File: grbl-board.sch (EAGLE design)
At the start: 29 parts, among them IC2 FT232RL, IC3 ADUM1250, IC4 LM2596S, X1 PN61729-S, X5 22-23-2021

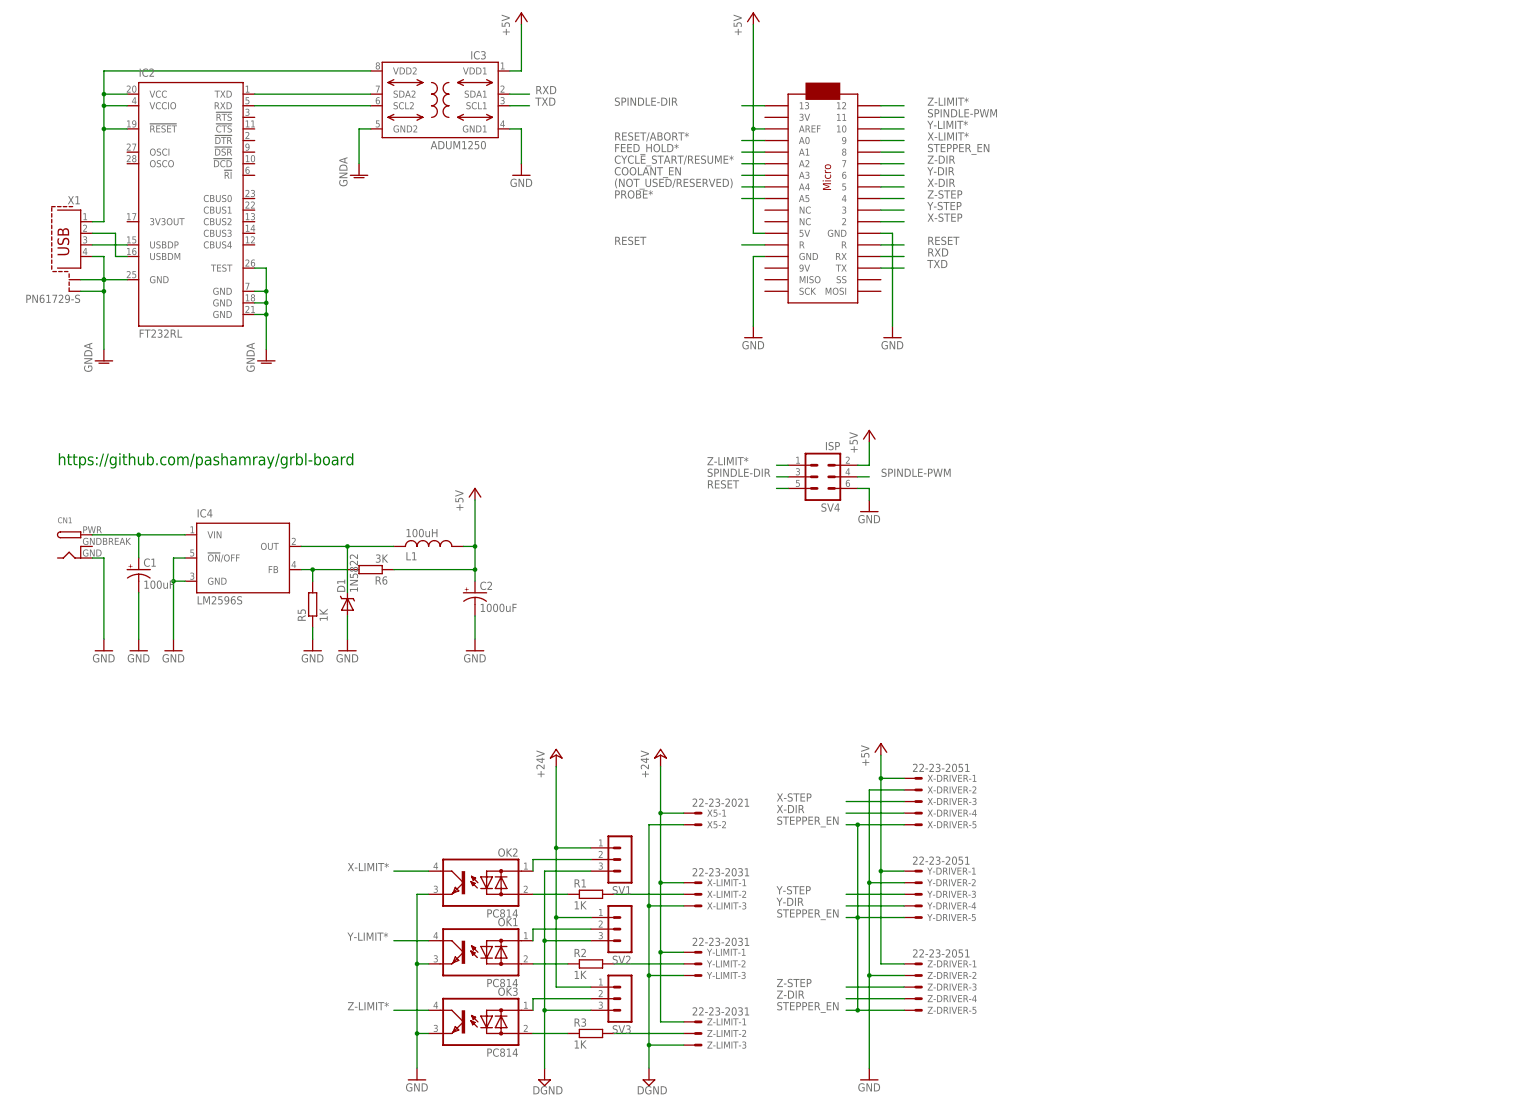
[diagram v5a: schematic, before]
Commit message: del arduino
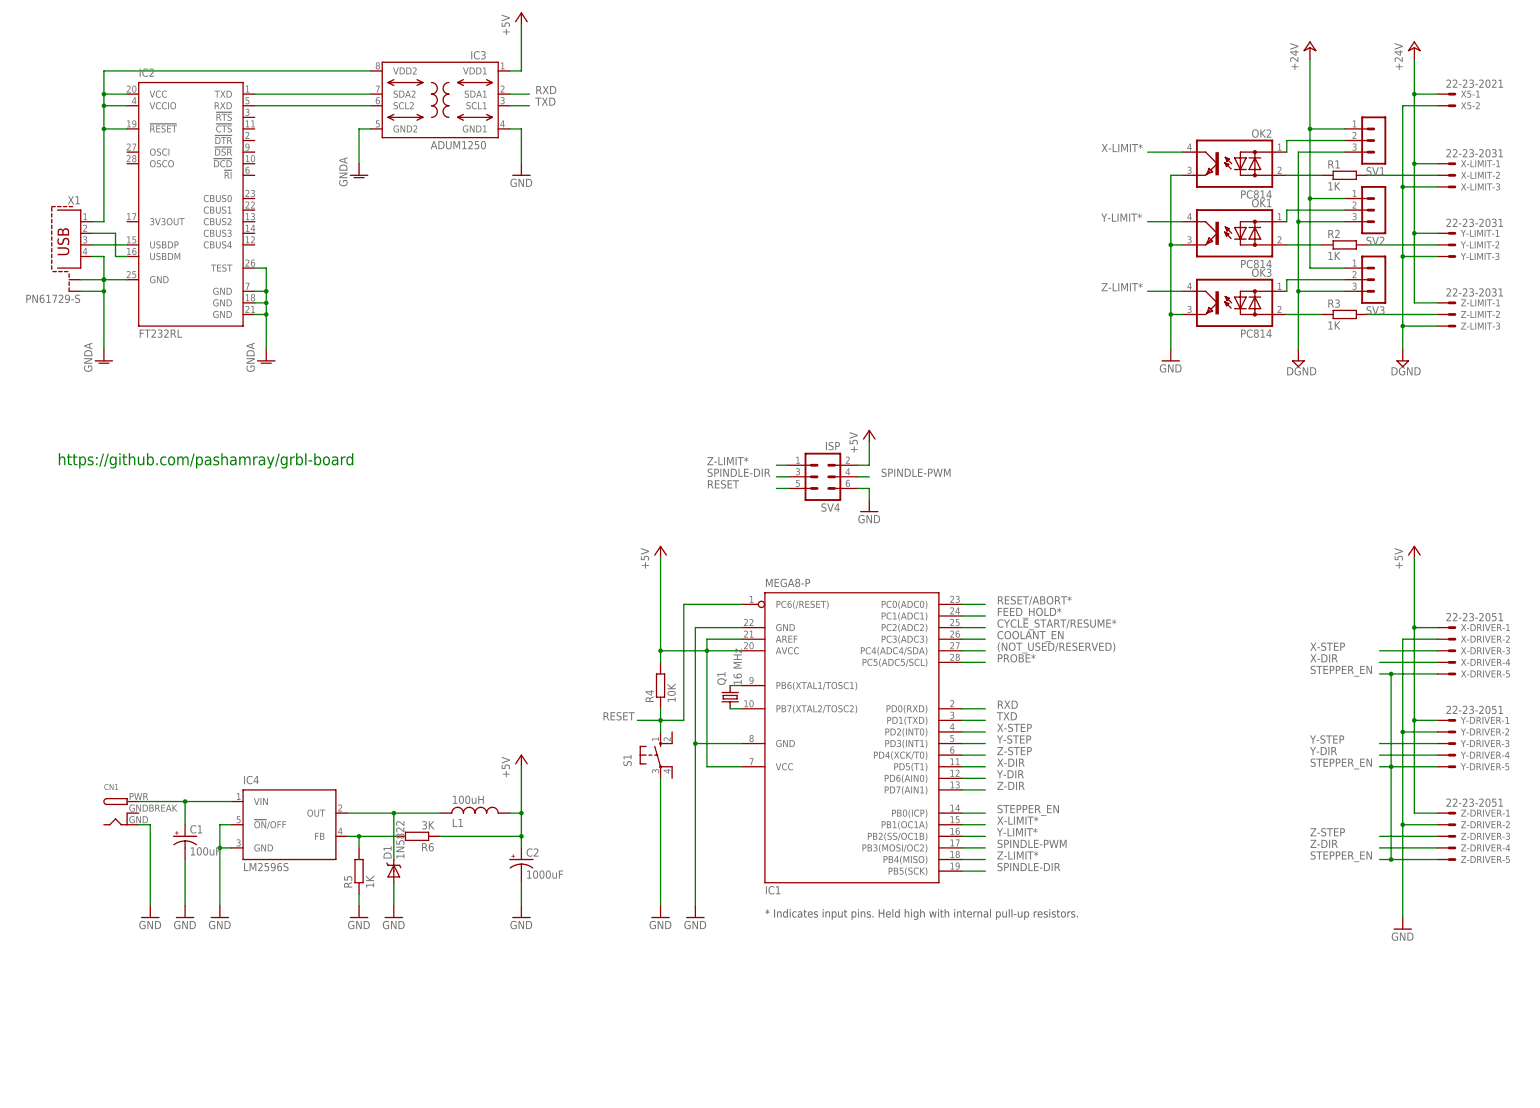
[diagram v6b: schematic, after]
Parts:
- removed U$1: ARDUINOMICRO, adafruit:ARDUINOMICRO
- added IC1: MEGA8-P, atmel:MEGA8-P
- added Q1: 16 MHz, crystal:CRYSTALHC49S
- added R4: 10K, resistor:R-EU_M0805
- added S1: (no value), switch-omron:10-XX
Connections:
- new net N$6: IC1.PB6(XTAL1/TOSC1), Q1.2
- new net N$7: IC1.PB7(XTAL2/TOSC2), Q1.1
- net (NOT_USED/RESERVED): now also IC1.PC4(ADC4/SDA); no longer U$1.A4
- net +5V: now also IC1.AREF, IC1.AVCC, IC1.VCC@1, R4.2; no longer U$1.5V, U$1.AREF
- net COOLANT_EN: now also IC1.PC3(ADC3); no longer U$1.A3
- net CYCLE_START/RESUME*: now also IC1.PC2(ADC2); no longer U$1.A2
- net FEED_HOLD*: now also IC1.PC1(ADC1); no longer U$1.A1
- net GND: now also IC1.GND, IC1.GND@1, S1.P; no longer U$1.GND, U$1.GND@1
- net PROBE*: now also IC1.PC5(ADC5/SCL); no longer U$1.A5
- net RESET: now also IC1.PC6(/RESET), R4.1, S1.S; no longer U$1.R@1, U$1.R@2
- net RESET/ABORT*: now also IC1.PC0(ADC0); no longer U$1.A0
- net RXD: now also IC1.PD0(RXD); no longer U$1.RX
- net SPINDLE-DIR: now also IC1.PB5(SCK); no longer U$1.13
- net SPINDLE-PWM: now also IC1.PB3(MOSI/OC2); no longer U$1.11
- net STEPPER_EN: now also IC1.PB0(ICP); no longer U$1.8
- net TXD: now also IC1.PD1(TXD); no longer U$1.TX
- net X-DIR: now also IC1.PD5(T1); no longer U$1.5
- net X-LIMIT*: now also IC1.PB1(OC1A); no longer U$1.9
- net X-STEP: now also IC1.PD2(INT0); no longer U$1.2
- net Y-DIR: now also IC1.PD6(AIN0); no longer U$1.6
- net Y-LIMIT*: now also IC1.PB2(SS/OC1B); no longer U$1.10
- net Y-STEP: now also IC1.PD3(INT1); no longer U$1.3
- net Z-DIR: now also IC1.PD7(AIN1); no longer U$1.7
- net Z-LIMIT*: now also IC1.PB4(MISO); no longer U$1.12
- net Z-STEP: now also IC1.PD4(XCK/T0); no longer U$1.4
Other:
- note added: "* Indicates input pins. Held high with internal pull-up resistors."
- moved on the sheet: C1, C2, CN1, D1, IC4, L1, OK1, OK2, OK3, R1, R2, R3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

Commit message: add buttons
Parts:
- removed S1: (no value), switch-omron:10-XX
- removed X5: 22-23-2021, con-molex:22-23-2021
- added 24V: 22-23-2021, con-molex:22-23-2021
- added FEED_HOLD, PROBE, RESET/ABORT, START/RESUME: 22-23-2031, con-molex:22-23-2031
- added OK4, OK5, OK6, OK7: PC814, optocoupler:PC814
- added R10, R7, R8, R9: 1K, resistor:R-EU_M0805
- added SV5, SV6, SV7, SV8: (no value), con-lstb:MA03-1
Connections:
- removed net VDD1: IC3.VDD1
- new net N$17: OK4.AC2, SV5.2
- new net N$20: OK4.AC1, R7.1
- new net N$21: OK5.AC2, SV6.2
- new net N$22: OK6.AC2, SV7.2
- new net N$23: OK7.AC2, SV8.2
- new net N$24: OK5.AC1, R8.1
- new net N$25: OK6.AC1, R9.1
- new net N$26: OK7.AC1, R10.1
- new net N$27: PROBE-1.S, R10.2
- new net N$28: R9.2, START/RESUME-1.S
- new net N$29: FEED_HOLD-1.S, R8.2
- new net N$30: R7.2, RESET/ABORT-1.S
- net +24V: now also 24V-1.S, FEED_HOLD-3.S, PROBE-3.S, RESET/ABORT-3.S, START/RESUME-3.S, SV5.1, SV6.1, SV7.1, SV8.1, X-LIMIT-3.S, Y-LIMIT-3.S, Z-LIMIT-3.S; no longer X-LIMIT-1.S, X5-1.S, Y-LIMIT-1.S, Z-LIMIT-1.S
- net +5V: now also IC3.VDD1
- net CYCLE_START/RESUME*: now also OK6.C
- net DGND: now also 24V-2.S, FEED_HOLD-2.S, PROBE-2.S, RESET/ABORT-2.S, START/RESUME-2.S, SV5.3, SV6.3, SV7.3, SV8.3, X-LIMIT-2.S, Y-LIMIT-2.S, Z-LIMIT-2.S; no longer X-LIMIT-3.S, X5-2.S, Y-LIMIT-3.S, Z-LIMIT-3.S
- net FEED_HOLD*: now also OK5.C
- net GND: now also OK4.E, OK5.E, OK6.E, OK7.E; no longer S1.P
- net N$10: now also R3.1; no longer SV3.2
- net N$11: now also OK3.AC2, SV3.2; no longer OK1.AC1, SV2.2
- net N$12: now also OK2.AC2; no longer OK2.AC1
- net N$13: now also X-LIMIT-1.S; no longer X-LIMIT-2.S
- net N$14: now also OK1.AC2, SV2.2; no longer OK3.AC2, R3.1
- net N$15: now also OK1.AC1; no longer OK1.AC2
- net N$5: now also OK2.AC1; no longer OK2.AC2
- net N$8: now also Y-LIMIT-1.S; no longer Y-LIMIT-2.S
- net N$9: now also Z-LIMIT-1.S; no longer Z-LIMIT-2.S
- net PROBE*: now also OK7.C
- net RESET: no longer S1.S
- net RESET/ABORT*: now also OK4.C
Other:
- moved on the sheet: OK1, OK2, OK3, R1, R2, R3, R4, SV1, SV2, SV3, X-LIMIT-1, X-LIMIT-2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

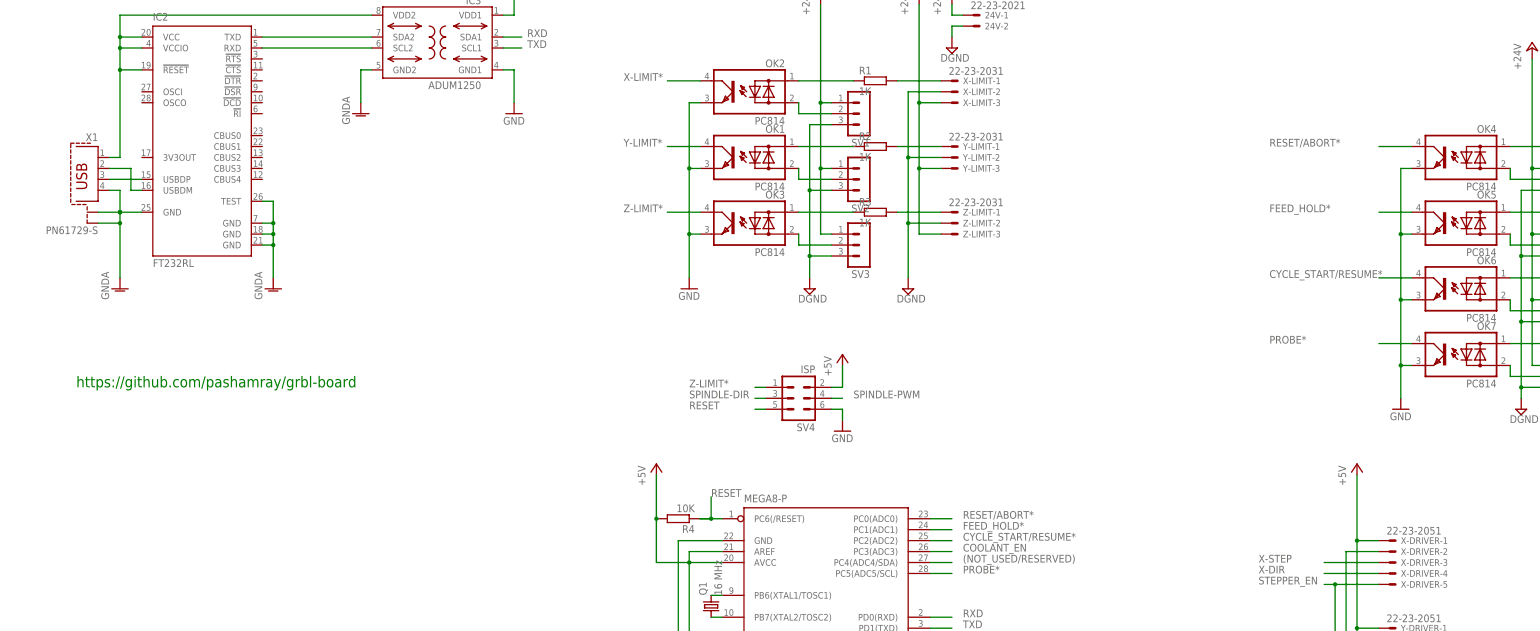
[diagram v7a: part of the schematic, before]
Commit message: add spindle
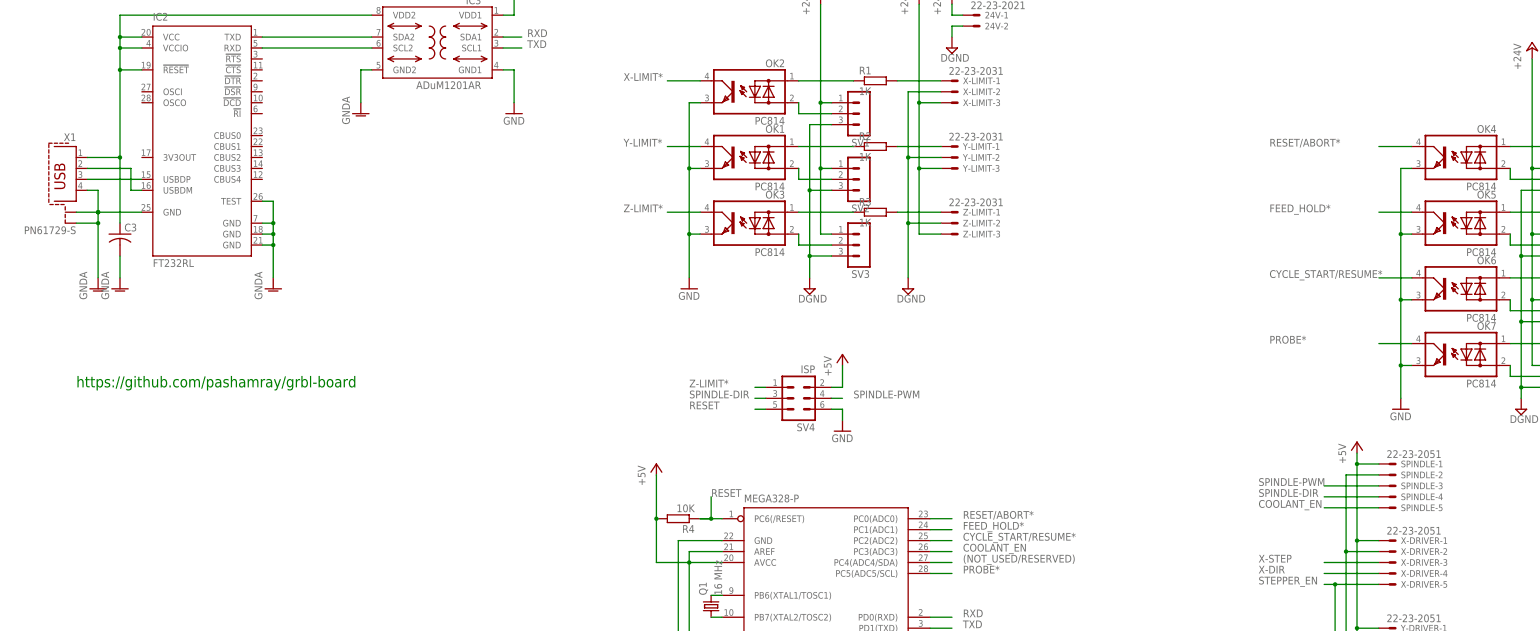
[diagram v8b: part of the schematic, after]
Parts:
- added C3: (no value), adafruit:C-USC0805K
- added SPINDLE: 22-23-2051, con-molex:22-23-2051
- C1, C2: device adafruit:CPOL-USE5-13 -> adafruit:CPOL-USE5-10.5
- IC1: value MEGA8-P -> MEGA328-P
- IC3: value ADUM1250 -> ADuM1201AR
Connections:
- removed net GND2: IC3.GND2
- net +5V: now also SPINDLE-1.S
- net COOLANT_EN: now also SPINDLE-5.S
- net GND: now also SPINDLE-2.S
- net GNDA: now also C3.2, IC3.GND2
- net SPINDLE-DIR: now also SPINDLE-4.S
- net SPINDLE-PWM: now also SPINDLE-3.S
- net VDD2: now also C3.1
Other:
- moved on the sheet: X1
